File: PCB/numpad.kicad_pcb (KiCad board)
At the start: 2 copper layers, 105.6 x 115.1 mm, 69 parts, among them J1 AVR-ISP-6, J2 Conn_01x04_Female, SW1 SW_Push, U1 ProMicro

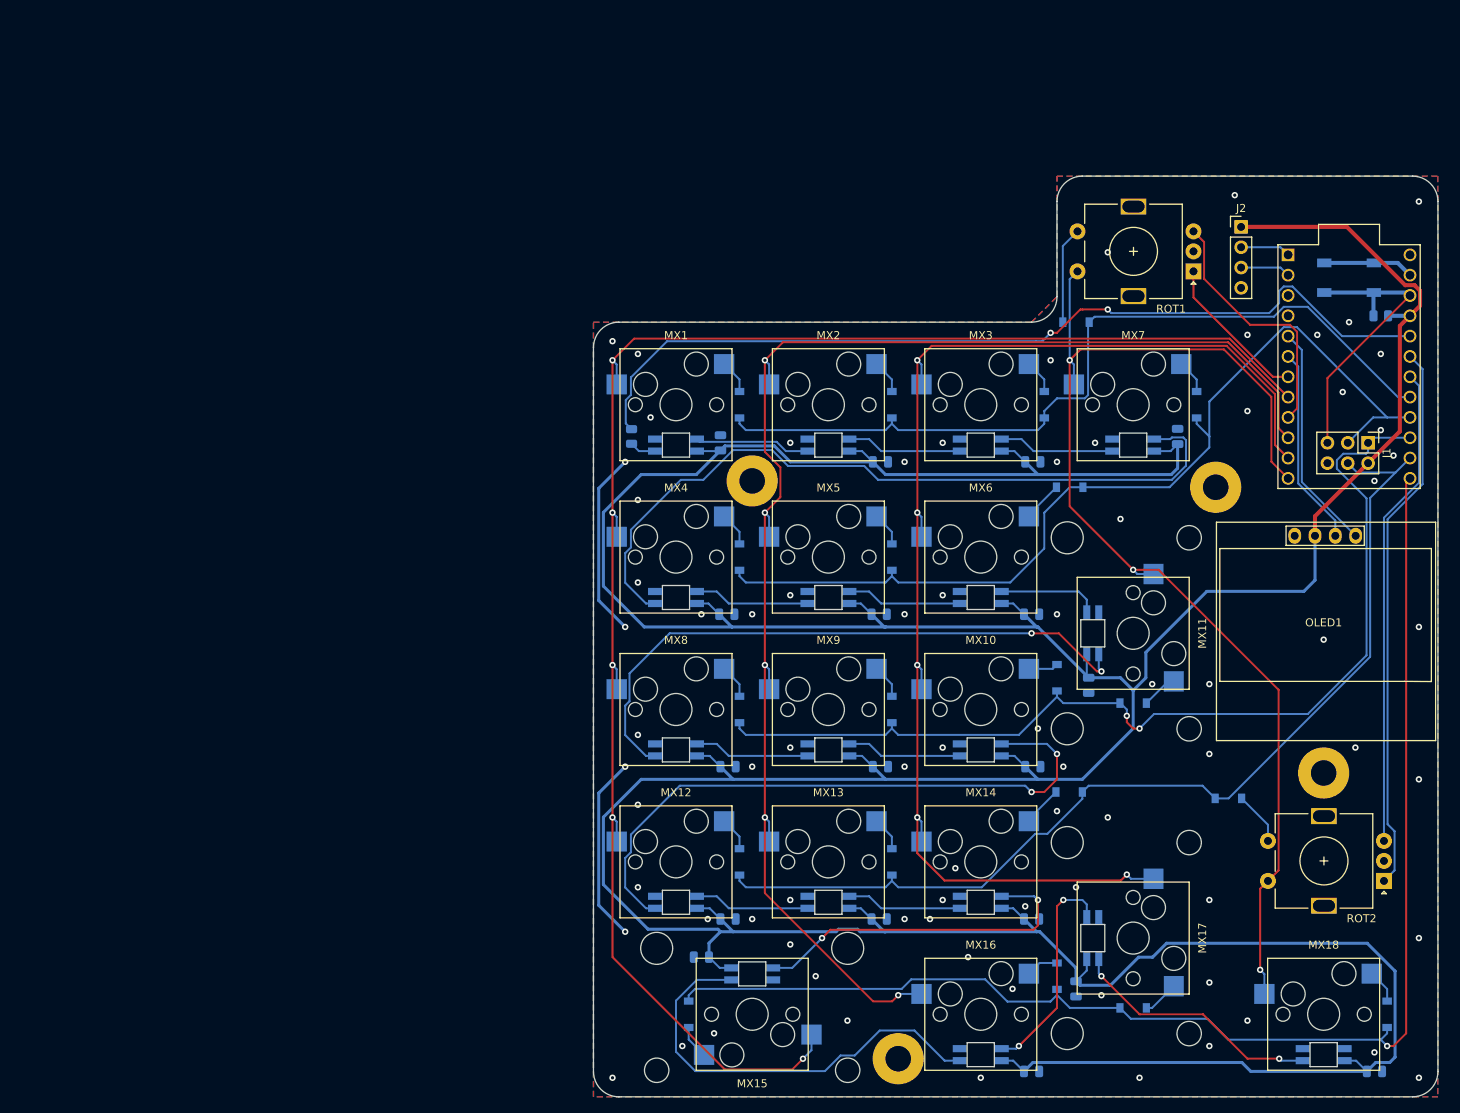
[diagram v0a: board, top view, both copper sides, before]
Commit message: Cleaned up traces
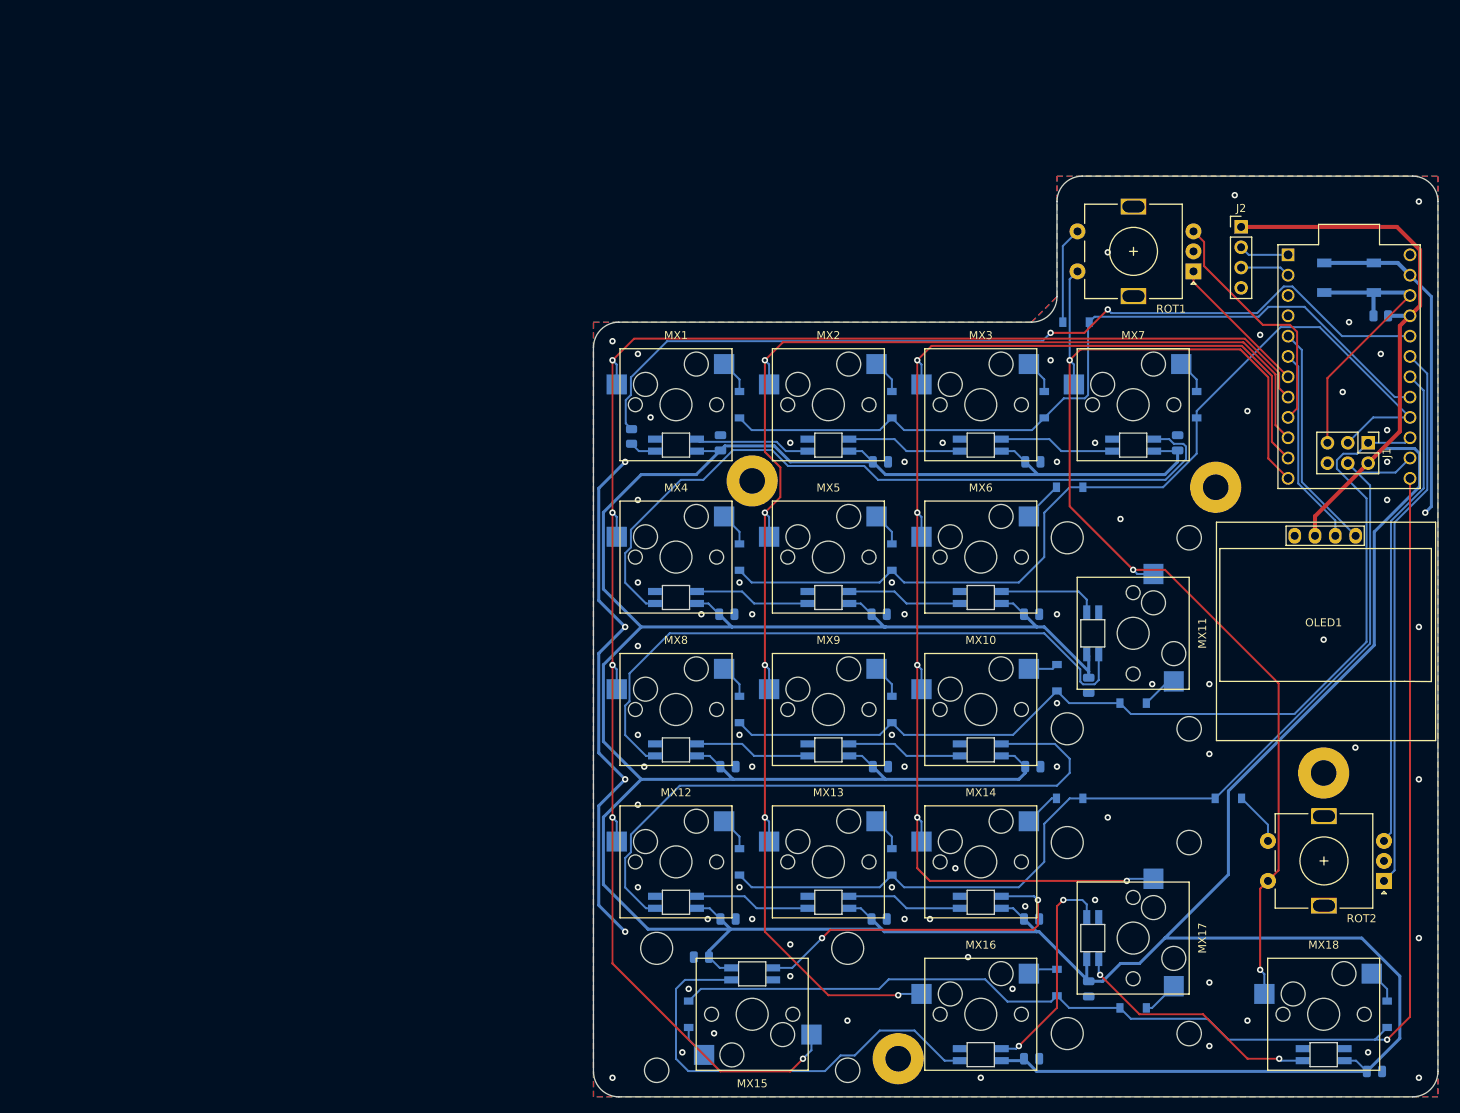
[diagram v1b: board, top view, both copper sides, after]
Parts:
- moved LC16 1.59 mm to (133.3, 170.6)
- moved LC17 1.59 mm to (140.5, 161.9)
- moved D14 0.80 mm to (138.1, 138.1)
- moved D16 0.79 mm to (136.5, 161.1)
- moved LC7 0.79 mm to (151.6, 93.7)
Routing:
- net GND: track 58.1 -> 109.4 mm, vias 79 -> 78
- net +5V: track 600.2 -> 638.9 mm
- net MISO: track 126.8 -> 122.0 mm, vias 2 -> 0
- net COL1: track 180.6 -> 183.9 mm
- net ROW4: track 168.2 -> 165.7 mm
- net DOUT3: track 78.1 -> 80.5 mm, vias 2 -> 0
- net COL2: track 162.6 -> 164.5 mm
- net COL0: track 209.8 -> 211.6 mm
- net DOUT4: track 79.1 -> 80.8 mm, vias 2 -> 0
- net COL3: track 149.8 -> 151.5 mm
- net ROW0: track 103.5 -> 102.0 mm
- net Net-(MX15-Pad5): track 54.5 -> 55.9 mm
- net MOSI: track 128.4 -> 127.2 mm
- net ENC_A1: track 19.2 -> 18.1 mm
- net DOUT1: track 94.9 -> 93.8 mm
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
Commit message: Polished routing
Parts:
- added MX19: MX-LED, CherryMX_PCB_KailhSocket:CherryMX_1.00u_PCB_KailhSocket, F.Cu at (15.1, 50.0)
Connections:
- MX18 pad 5: Net-(MX18-Pad5) -> (no net)
- U1 pad 24: Net-(U1-Pad24) -> (no net)
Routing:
- net DOUT1: track 93.8 -> 94.6 mm
- net DOUT4: track 80.8 -> 81.6 mm
- net BKL_DATA_IN: track 112.1 -> 112.8 mm

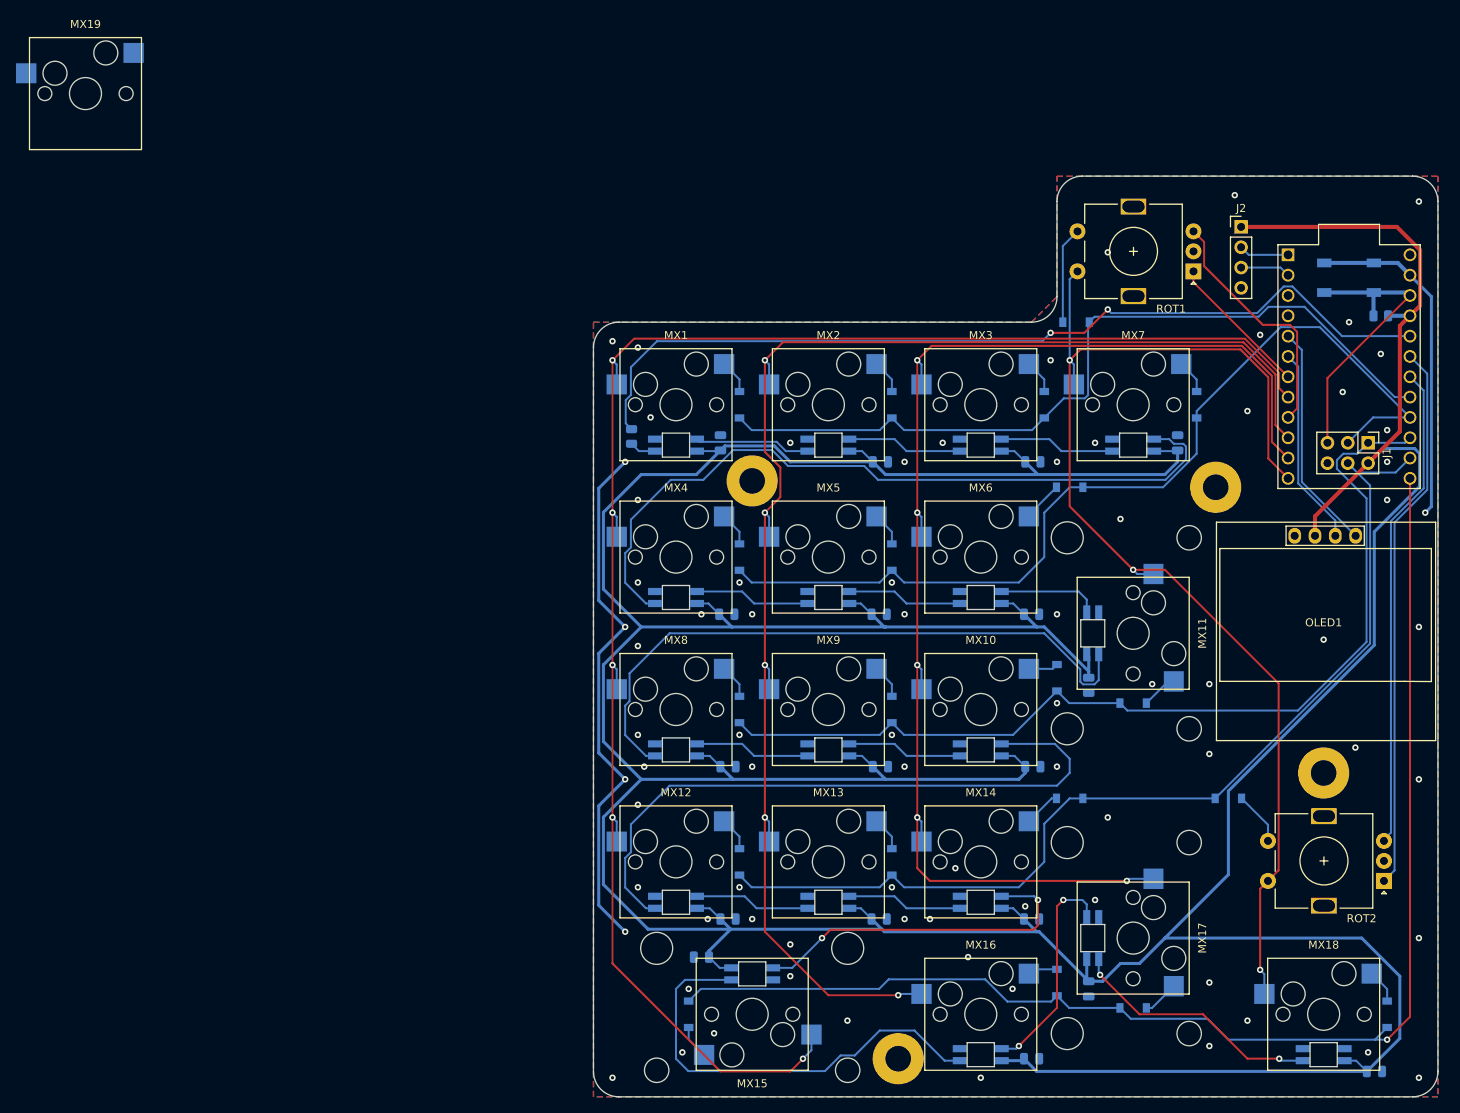
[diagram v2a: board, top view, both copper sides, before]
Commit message: Added logos, cleaned up routing
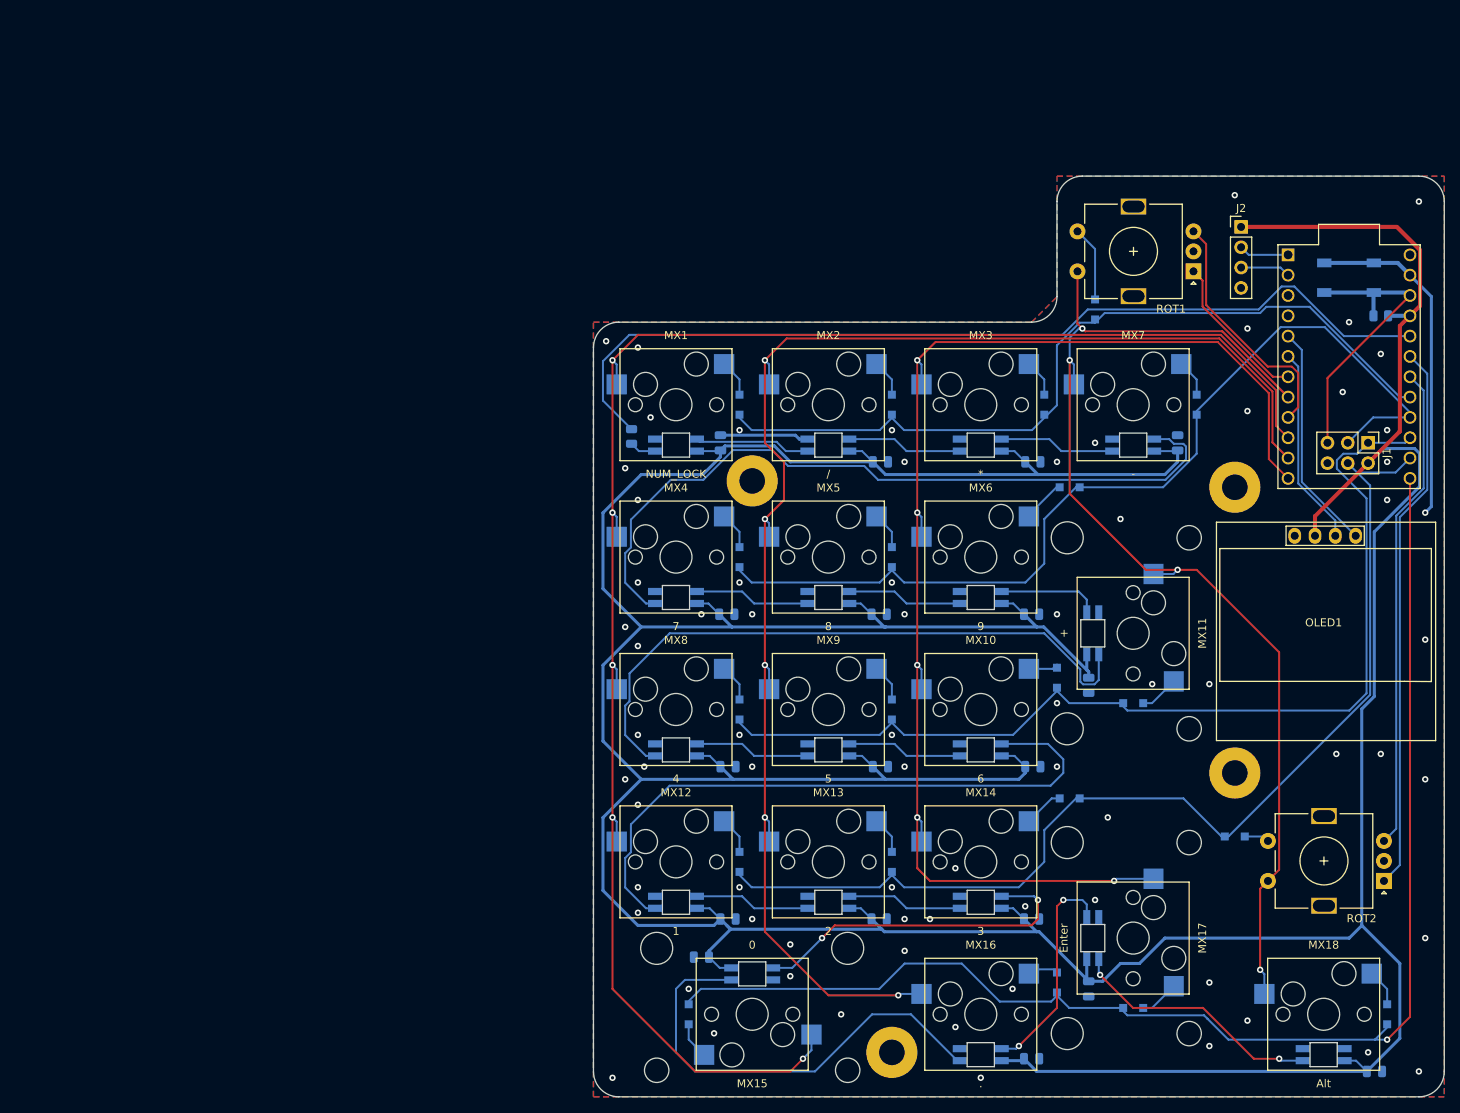
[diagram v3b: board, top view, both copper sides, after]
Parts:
- removed MX19: MX-LED, CherryMX_PCB_KailhSocket:CherryMX_1.00u_PCB_KailhSocket
- added LOGO1: Logo_Open_Hardware_Small, custom_footprints:logo, F.Cu at (178.6, 110.3)
- added LOGO2: Logo_Open_Hardware_Small, custom_footprints:qmk_logo, B.Cu at (177.8, 125.4)
- added LOGO3: Logo_Open_Hardware_Small, custom_footprints:vial_logo, B.Cu at (163.5, 123.8)
- D1, D10, D11, D12, D13, D14, D15, D16, D17, D18, D2, D3, D4, D5, D6, D7, D8, D9, RD1, RD2: footprint Diode_SMD:D_SOD-123 -> Diode_SMD:D_SOD-323_HandSoldering
- MX18: value Backspace -> Alt; footprint CherryMX_PCB_KailhSocket_LTST-A683CEGBW:CherryMX_1.00u_PCB_KailhSocket_LTST-A683CEGBW -> CherryMX_PCB_KailhSocket_LTST-A683CEGBW:CherryMX_1.50u_PCB_KailhSocket_LTST-A683CEGBW
- moved H2 11.1 mm to (158.8, 134.9)
- moved RD2 4.83 mm to (158.7, 142.9)
- moved RD1 2.86 mm to (141.3, 77.0), turned to 90 degrees
- moved H3 2.39 mm to (158.8, 99.2)
- moved H1 1.12 mm to (115.9, 169.9)
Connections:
- U1 pad 10: COL1 -> COL0
- U1 pad 11: COL2 -> COL1
- U1 pad 12: COL3 -> COL2
- U1 pad 8: COL0 -> COL3
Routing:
- net GND: track 109.4 -> 53.6 mm, vias 78 -> 74
- net +5V: track 638.9 -> 629.7 mm
- net COL3: track 151.5 -> 143.0 mm, vias 3 -> 4
- net MOSI: track 127.2 -> 134.4 mm
- net COL0: track 211.6 -> 217.4 mm
- net BKL_DATA_IN: track 112.8 -> 117.3 mm, vias 2 -> 0
- net Net-(RD2-Pad2): track 6.68 -> 2.73 mm
- net MISO: track 121.7 -> 125.4 mm
- net Net-(RD1-Pad2): track 12.3 -> 9.02 mm
- net ROW4: track 165.7 -> 167.3 mm
- net DOUT4: track 81.6 -> 80.0 mm
- net COL2: track 164.5 -> 165.9 mm
- net Net-(MX15-Pad5): track 55.9 -> 57.2 mm
- net ENC_A1: track 18.1 -> 19.2 mm
- net COL1: track 183.9 -> 184.9 mm
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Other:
- board size 105.6 x 115.1 mm -> 106.4 x 115.1 mm
- board text added: "howardt12345.com"
- board text added: "kb.ht12345.xyz/numpad"
- board text added: "numpad prototype 1"
- board text added: "© 2022 Howard Tseng"

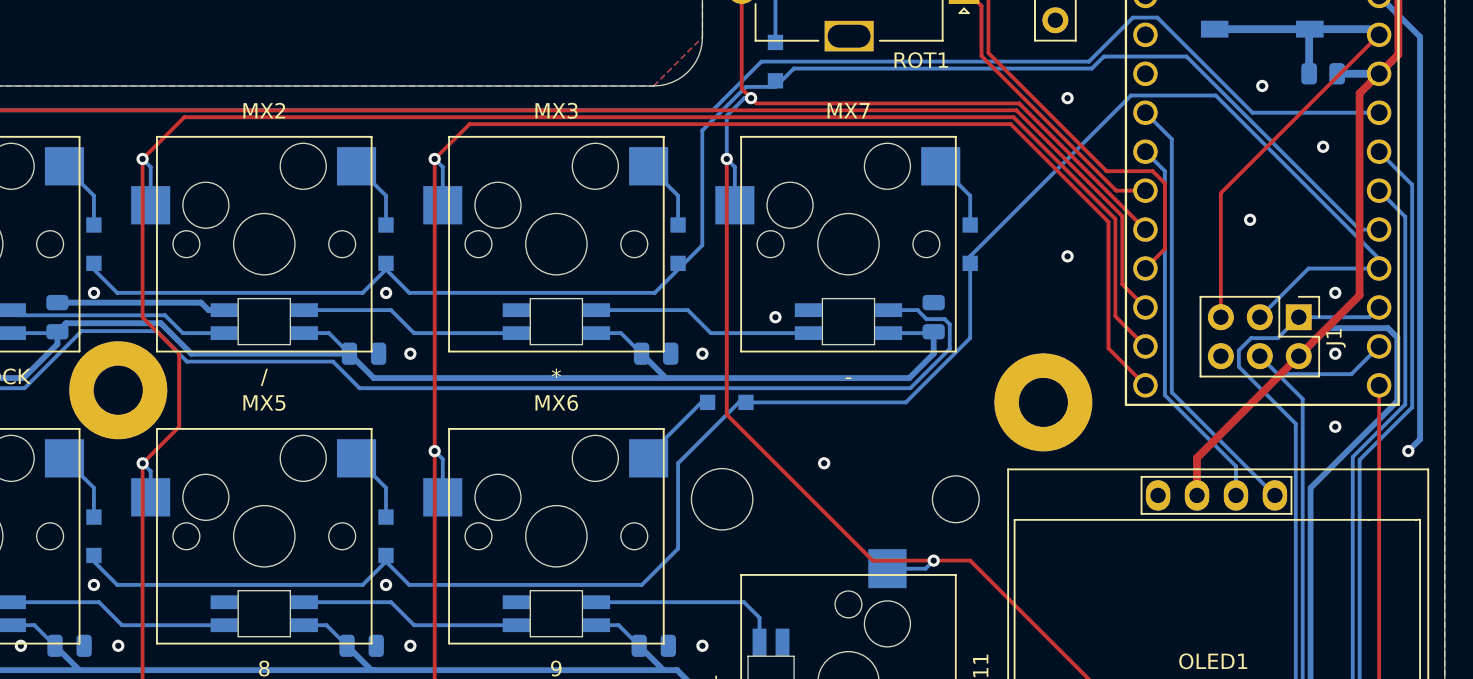
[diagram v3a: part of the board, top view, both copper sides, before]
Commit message: Moved order number and exported production gerbers
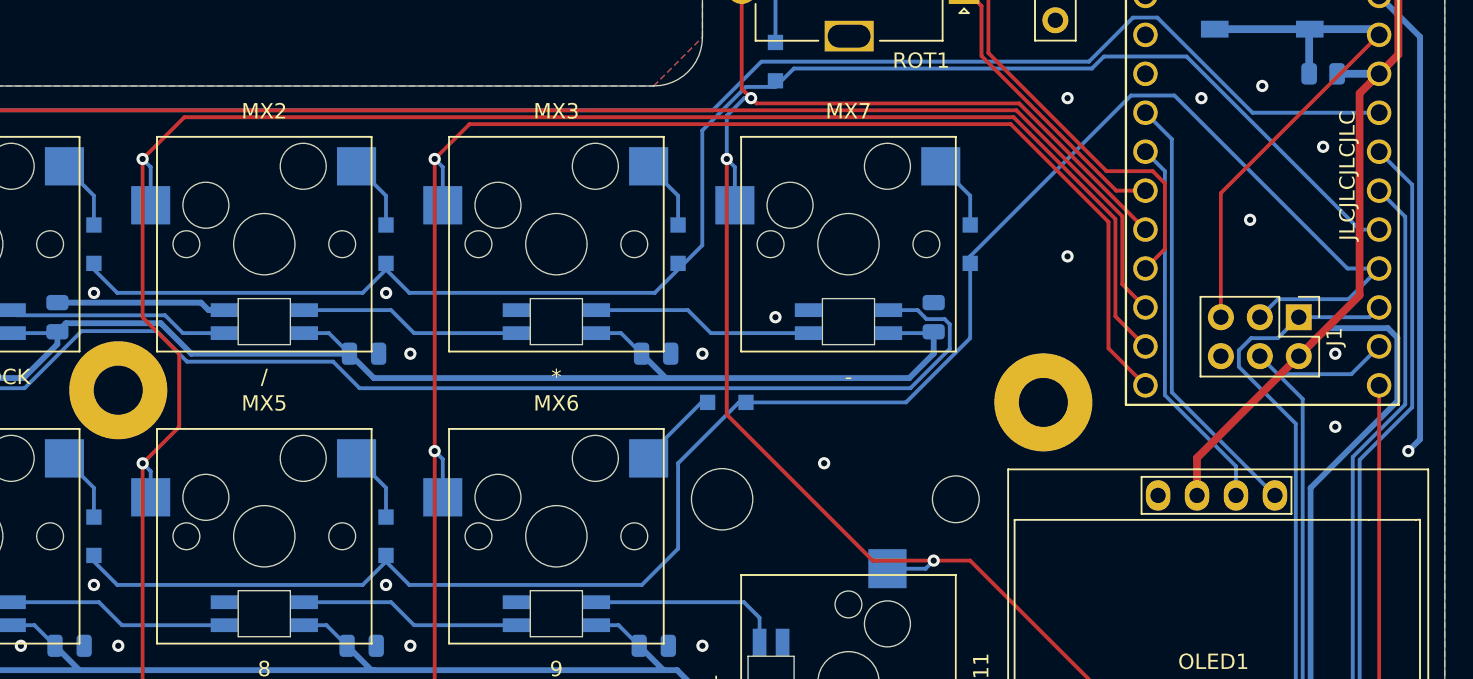
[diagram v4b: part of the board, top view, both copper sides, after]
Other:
- board text added: "JLCJLCJLCJLC"
